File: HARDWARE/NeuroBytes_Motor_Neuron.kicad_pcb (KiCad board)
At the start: 2 copper layers, 52.6 x 28.8 mm, 25 parts, among them P1 CONN_01X04, P12 CONN_01X07, P2 CONN_01X04, P3 CONN_01X04, P4 CONN_01X03, P5 CONN_01X03, Q1 NPN_dual, Q2 NPN_dual, SW1 SW_PUSH, U1 STM32L011Gx, U2 LD3985G33R

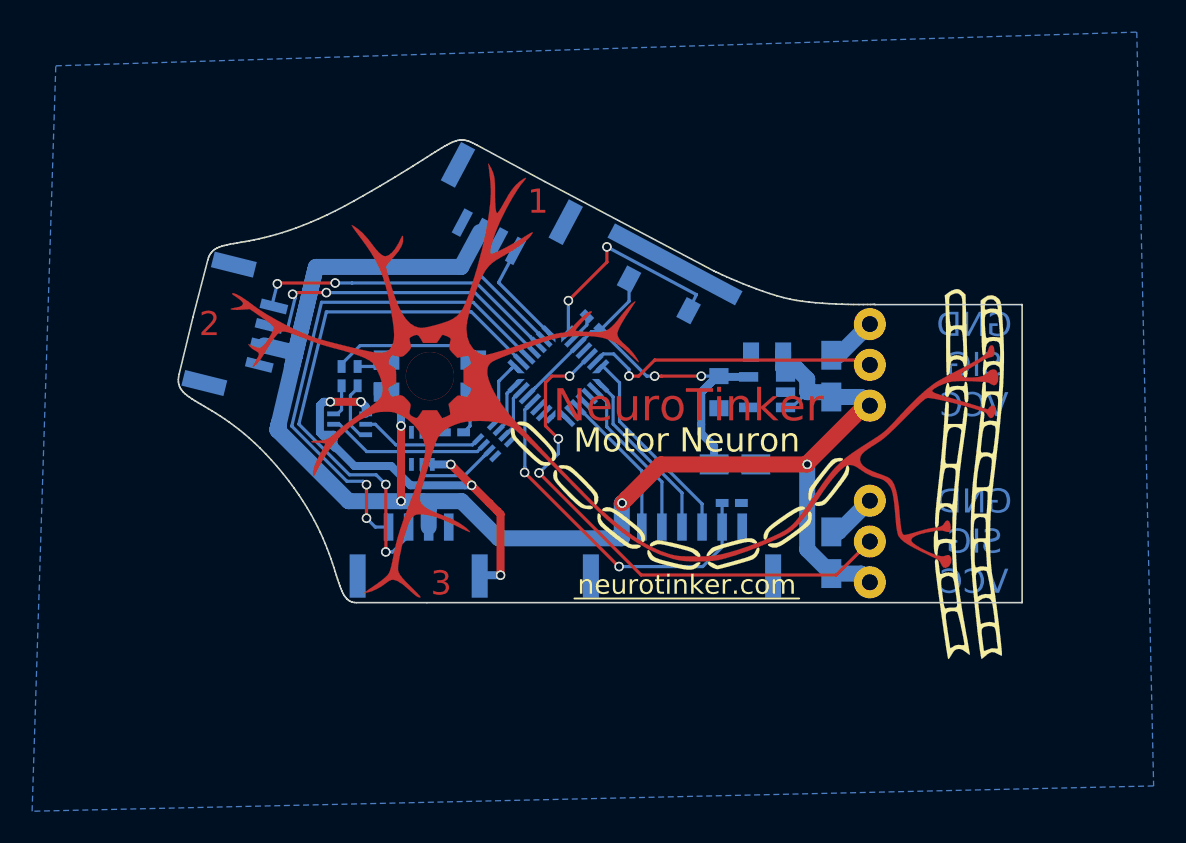
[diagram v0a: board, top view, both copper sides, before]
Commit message: Hardware v3. Changed headers to 3-position JST GH headers. Modified graphics and PCB outline -- now convex-ish, and includes parallel faces for V-scoring and routing.
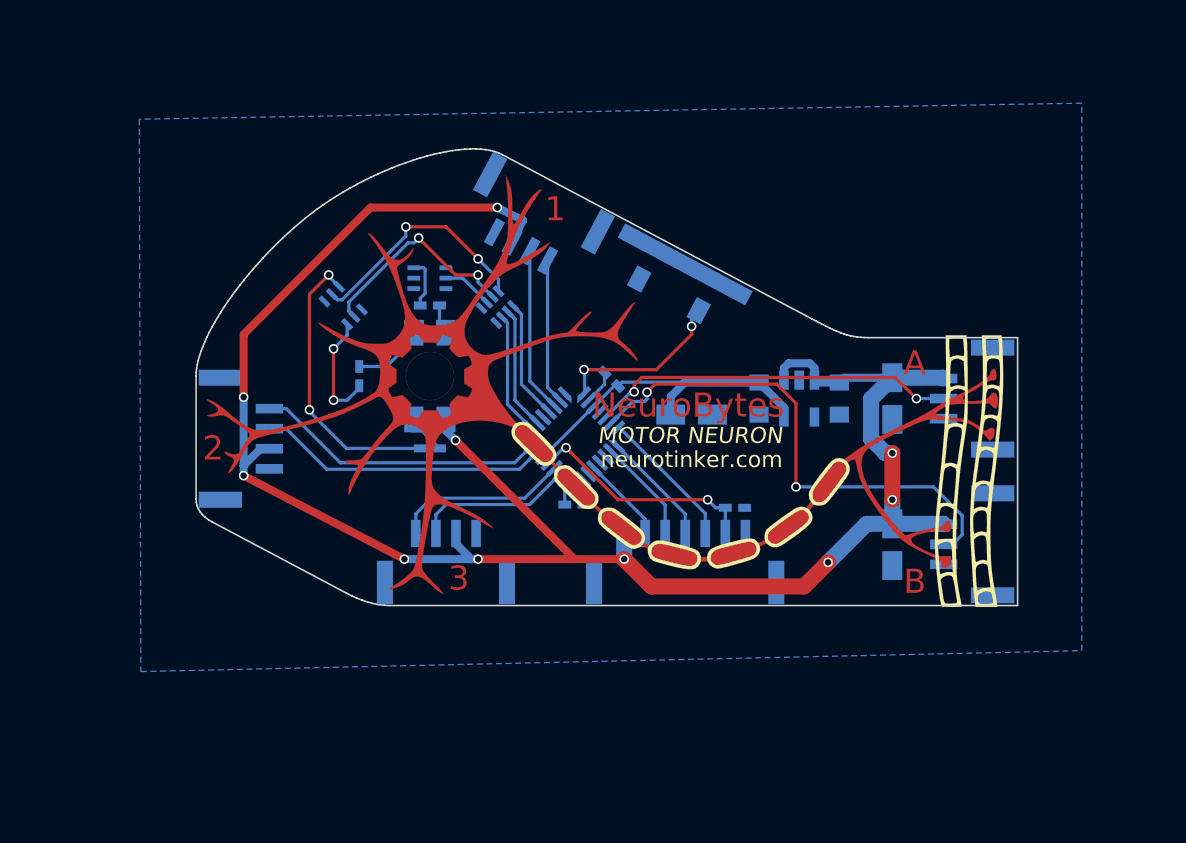
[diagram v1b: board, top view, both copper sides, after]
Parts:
- removed the G*** at (177.0, 58.0)
- removed the G*** at (201.0, 66.0)
- added G***: LOGO, KiCad_Footprints:ZF_LOGO_Motor_Neuron, F.Cu at (177.0, 58.0)
- added R4: R, KiCad_Footprints:ZF_SMD_NonPol_0402, B.Cu at (186.0, 66.0)
- P4, P5: footprint KiCad_Footprints:ZF_CONN_1x3_servo -> KiCad_Footprints:ZF_CONN_JST_GH_3POS; moved to B.Cu
- moved P5 13.2 mm to (211.4, 68.5), turned to 0 degrees
- moved P4 11.3 mm to (211.4, 59.4), turned to 0 degrees
- moved Q1 10.6 mm to (177.0, 51.9), turned to 270 degrees
- moved RN1 8.30 mm to (181.2, 53.7), turned to 135 degrees
- moved R1 8.04 mm to (177.0, 53.6)
- moved Q2 7.41 mm to (171.6, 53.6), turned to 225 degrees
- moved P2 7.00 mm to (164.6, 61.9), turned to 180 degrees
- moved R3 6.36 mm to (177.0, 62.5), turned to 180 degrees
- moved C1 5.35 mm to (202.5, 59.4), turned to 270 degrees
- moved C2 4.11 mm to (193.3, 60.4)
- moved C6 4.05 mm to (205.8, 59.4), turned to 270 degrees
- moved U1 3.93 mm to (186.0, 61.8)
- moved C7 3.83 mm to (205.8, 68.5), turned to 270 degrees
- moved C3 3.67 mm to (188.3, 58.2)
- moved C4 2.53 mm to (197.5, 59.4)
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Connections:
- SW1 pad 1: +3V3 -> GND
- U1 pad 10: D3EX -> Net-(U1-Pad10)
- U1 pad 11: D2IN -> LED_G
- U1 pad 12: D2EX -> D1IN
- U1 pad 13: D1IN -> D1EX
- U1 pad 14: D1EX -> Net-(U1-Pad14)
- U1 pad 2: Net-(U1-Pad2) -> D3IN
- U1 pad 3: Net-(U1-Pad3) -> D3EX
- U1 pad 6: LED_R -> D2IN
- U1 pad 7: LED_B -> D2EX
- U1 pad 8: LED_G -> LED_R
- U1 pad 9: D3IN -> LED_B
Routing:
- net GND: track 36.6 -> 2.14 mm, vias 5 -> 0
- net D3IN: track 34.2 -> 9.96 mm, vias 2 -> 0
- net D3EX: track 32.0 -> 11.0 mm, vias 2 -> 0
- net Net-(Q2-Pad6): track 3.83 -> 17.9 mm, vias 0 -> 2
- net +5V: track 104.3 -> 118.1 mm, vias 4 -> 10
- net SERVO_2: track 18.7 -> 32.2 mm, vias 1 -> 2
- net SERVO_1: track 34.0 -> 22.9 mm, vias 3 -> 2
- net +3V3: track 28.7 -> 20.5 mm, vias 2 -> 0
- net RESET: track 22.6 -> 14.5 mm
- net Net-(Q2-Pad5): track 7.69 -> 14.8 mm, vias 0 -> 2
- net Net-(Q2-Pad3): track 2.10 -> 7.14 mm, vias 0 -> 2
- net LED_B: track 3.12 -> 7.71 mm
- net LED_R: track 3.27 -> 7.56 mm
- net SWCLK/MISO: track 11.2 -> 7.08 mm
- net Net-(D1-Pad4): track 8.83 -> 4.80 mm
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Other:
- board size 52.6 x 28.8 mm -> 51.2 x 28.4 mm
- board text added: "A"
- board text added: "B"
- board text added: "ID"
- board text added: "MOTOR NEURON"
- board text added: "NeuroBytes"
- board text removed: "GND"
- board text removed: "Motor Neuron"
- board text removed: "NeuroTinker"
- board text removed: "SIG"
- board text removed: "VCC"

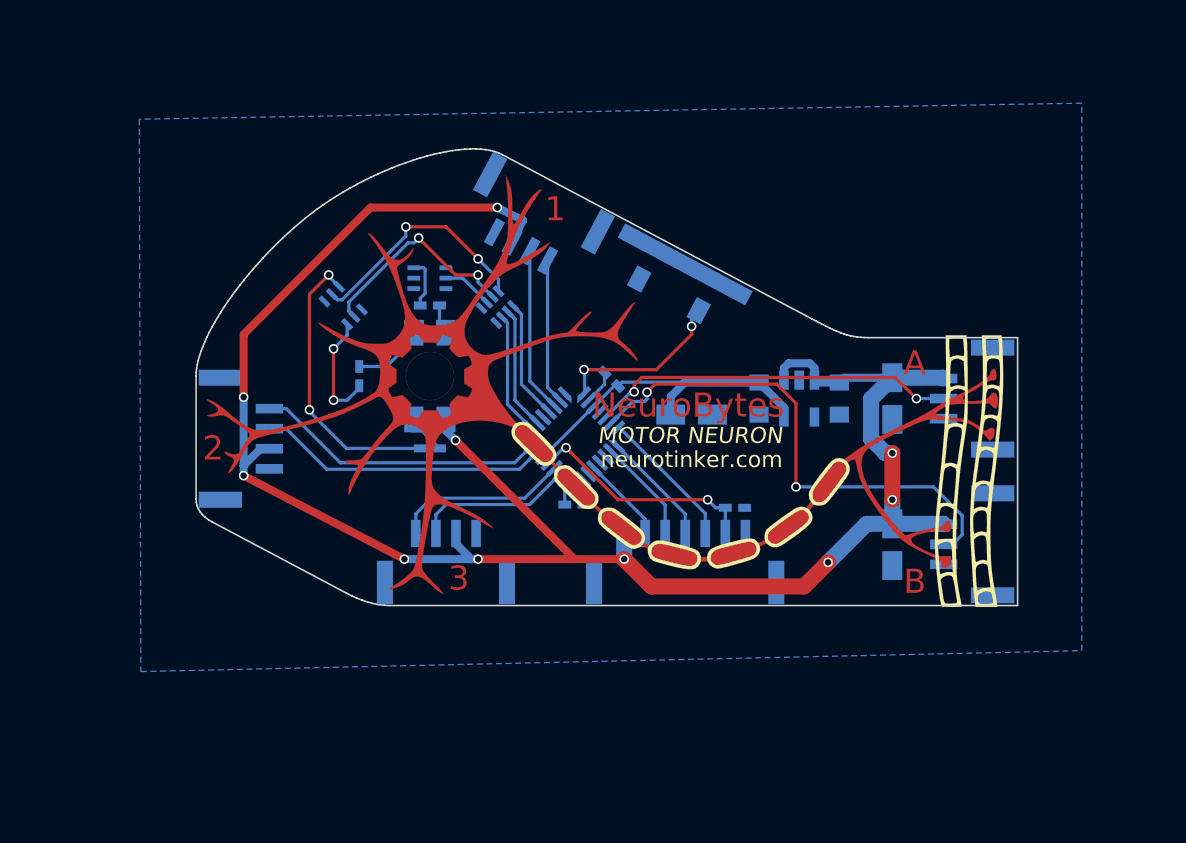
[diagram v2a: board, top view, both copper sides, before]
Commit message: updated switch and header footprints. changed to nonpolarized tank caps. split resistor network and dual transistors into discrete components. other minor tweaks.
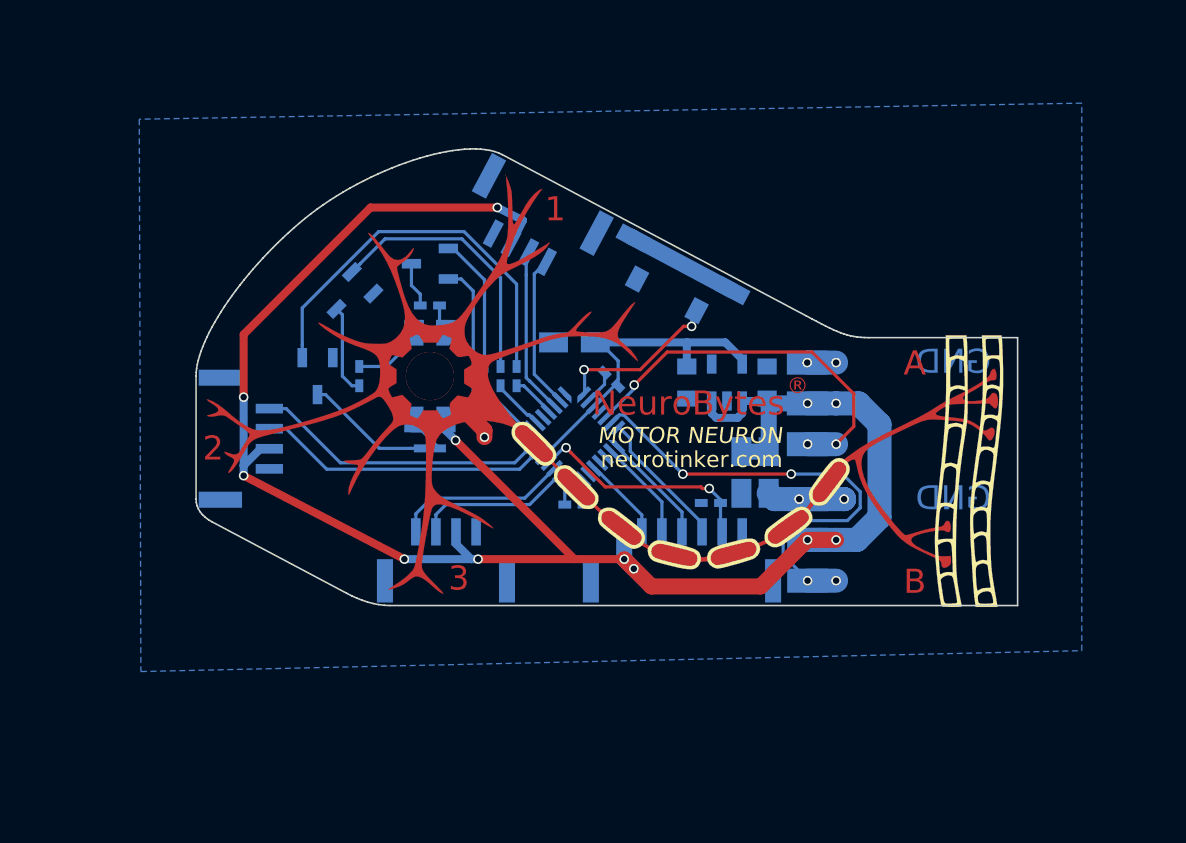
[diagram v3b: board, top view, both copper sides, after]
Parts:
- removed RN1: R_Pack04, KiCad_Footprints:ZF_RN_4iso_CTS-0804
- added Q3: MMBT3904, KiCad_Footprints:ZF_SOT23-3L, B.Cu at (170.0, 58.0)
- added R5: 1k, KiCad_Footprints:ZF_SMD_NonPol_0402, B.Cu at (180.4, 58.0)
- added R6: 1k, KiCad_Footprints:ZF_SMD_NonPol_0402, B.Cu at (181.4, 58.0)
- added R7: 1k, KiCad_Footprints:ZF_SMD_NonPol_0402, B.Cu at (182.4, 58.0)
- C2, C6, C7: value CP -> C; footprint KiCad_Footprints:ZF_SMD_pol_1206 -> KiCad_Footprints:ZF_SMD_nonpol_1206
- P1, P2, P3: value CONN_01X04 -> JST_GH_4POS
- P12: value CONN_01X07 -> JST_GH_7POS
- P4, P5: value CONN_01X03 -> SERVO_CONN; footprint KiCad_Footprints:ZF_CONN_JST_GH_3POS -> KiCad_Footprints:ZF_CONN_SERVO_HDR_SMT
- Q1, Q2: value NPN_dual -> MMBT3904; footprint KiCad_Footprints:ZF_SMD_SOT-363 -> KiCad_Footprints:ZF_SOT23-3L
- R1: value R -> 220
- R2, R3: value R -> 100
- moved P4 10.9 mm to (200.5, 59.7)
- moved P5 10.9 mm to (200.5, 68.2)
- moved C6 10.5 mm to (196.4, 64.0)
- moved C7 8.92 mm to (198.1, 64.0)
- moved C2 8.58 mm to (186.0, 55.9), turned to 180 degrees
- moved C1 4.61 mm to (198.0, 58.4), turned to 90 degrees
- moved C4 4.61 mm to (193.0, 58.4)
- moved U2 4.61 mm to (195.5, 58.4), turned to 180 degrees
- moved SW1 1.77 mm to (192.2, 52.1)
- moved C5 1.53 mm to (194.5, 65.9), turned to 180 degrees
- moved P12 0.92 mm to (192.7, 69.3)
- moved Q1 0.90 mm to (177.0, 51.0), turned to 90 degrees
- moved P1 0.81 mm to (183.4, 48.5)
- moved P3 0.80 mm to (178.0, 69.4)
- moved Q2 0.72 mm to (172.0, 53.0), turned to 135 degrees
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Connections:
- net SWITCH renamed IDENTIFY
- P4 pad 1: +5V -> GND
- P4 pad 2: SERVO_1 -> +5V
- P4 pad 3: GND -> SERVO_1
- P5 pad 1: +5V -> GND
- P5 pad 2: SERVO_2 -> +5V
- P5 pad 3: GND -> SERVO_2
- Q1 pad 1: GND -> Net-(Q1-Pad1)
- Q1 pad 2: Net-(Q1-Pad2) -> GND
- Q2 pad 1: GND -> Net-(Q2-Pad1)
- Q2 pad 2: Net-(Q2-Pad2) -> GND
- R1 pad 2: Net-(Q1-Pad6) -> Net-(Q1-Pad3)
- R3 pad 2: Net-(Q2-Pad6) -> Net-(Q3-Pad3)
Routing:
- net GND: track 2.14 -> 29.9 mm, vias 0 -> 5
- net Net-(Q3-Pad1): track 0.00 -> 24.9 mm
- net Net-(Q2-Pad6): track 17.9 -> 0.00 mm, vias 2 -> 0
- net Net-(Q2-Pad1): track 0.00 -> 16.7 mm
- net Net-(Q2-Pad5): track 14.8 -> 0.00 mm, vias 2 -> 0
- net Net-(Q2-Pad2): track 13.5 -> 0.00 mm, vias 2 -> 0
- net Net-(Q1-Pad1): track 0.00 -> 8.46 mm
- net Net-(Q3-Pad3): track 0.00 -> 7.79 mm
- net LED_G: track 7.50 -> 2.70 mm
- net LED_B: track 7.71 -> 3.35 mm
- net LED_R: track 7.56 -> 3.99 mm
- net Net-(Q1-Pad2): track 3.19 -> 0.00 mm
- net Net-(Q1-Pad6): track 3.12 -> 0.00 mm
- net Net-(Q1-Pad3): track 0.00 -> 2.83 mm
- net SERVO_2: track 32.2 -> 29.9 mm, vias 2 -> 4
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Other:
- net class Default: clearance 0.2 -> 0.15
- rule trace_clearance: 0.2 -> 0.15
- board text added: "GND"
- board text added: "®"
- board text removed: "SERVOS"

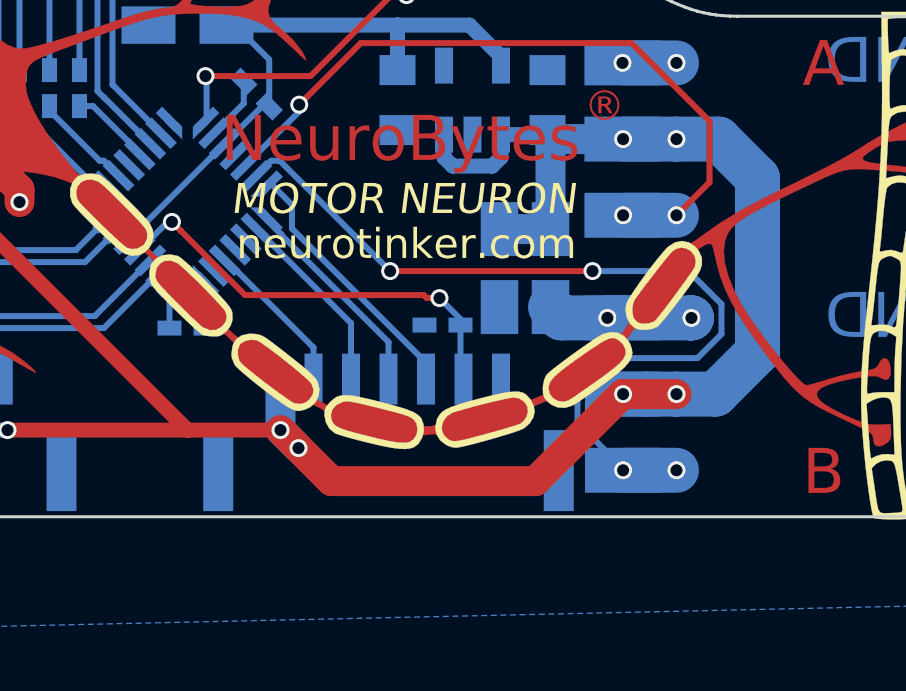
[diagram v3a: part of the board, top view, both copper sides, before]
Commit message: changed to 5-pin JST GH connector for power and programming. Added POWER label and increased ID label size to standard (1.2 / 0.17). Minor routing and labeling updates.
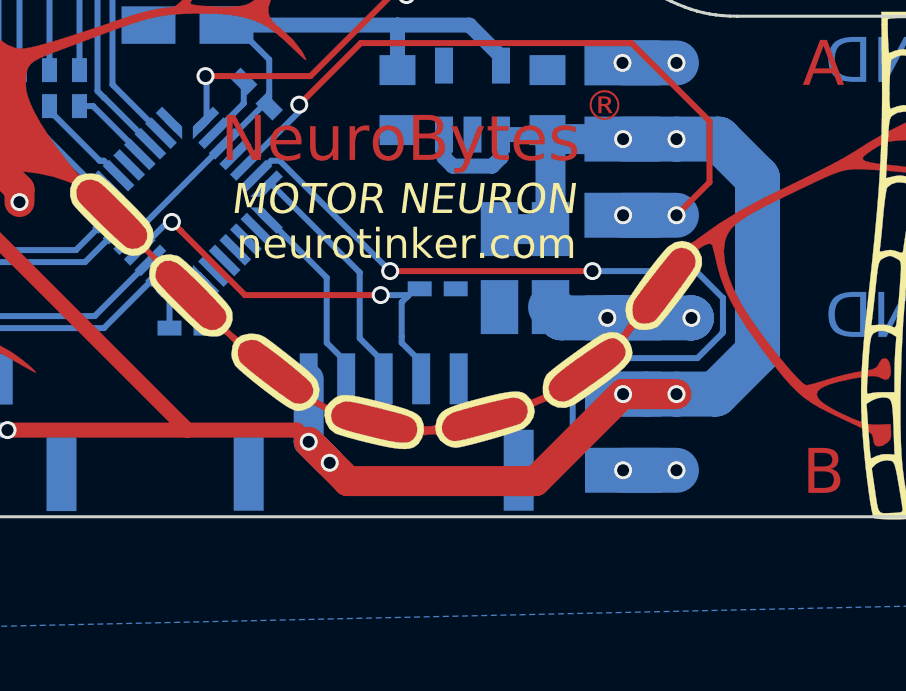
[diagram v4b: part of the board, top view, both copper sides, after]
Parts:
- removed P12: JST_GH_7POS, KiCad_Footprints:ZF_CONN_JST_GH_7POS
- added P6: JST_GH_5-pos, KiCad_Footprints:ZF_CONN_JST_GH_5POS, B.Cu at (192.5, 69.3)
- moved C5 1.22 mm to (194.3, 64.7), turned to 0 degrees
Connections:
- U1 pad 21: SWDIO/SCK -> SWDIO
- U1 pad 22: SWCLK/MISO -> SWCLK
- U1 pad 23: NSS -> Net-(U1-Pad23)
- U1 pad 26: MOSI -> Net-(U1-Pad26)
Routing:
- net SWDIO/SCK: track 8.69 -> 0.00 mm
- net SWDIO: track 0.00 -> 8.09 mm
- net SWCLK/MISO: track 6.90 -> 0.00 mm
- net SWCLK: track 0.00 -> 6.37 mm
- net NSS: track 6.32 -> 0.00 mm
- net MOSI: track 5.22 -> 0.00 mm
- net SERVO_2: track 29.9 -> 30.5 mm
- net +5V: track 120.3 -> 120.9 mm
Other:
- net class Default: clearance 0.15 -> 0.2
- rule trace_clearance: 0.15 -> 0.2
- board text added: "POWER"
- board text added: "SIG"
